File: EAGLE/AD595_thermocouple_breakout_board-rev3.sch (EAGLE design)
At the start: 7 parts

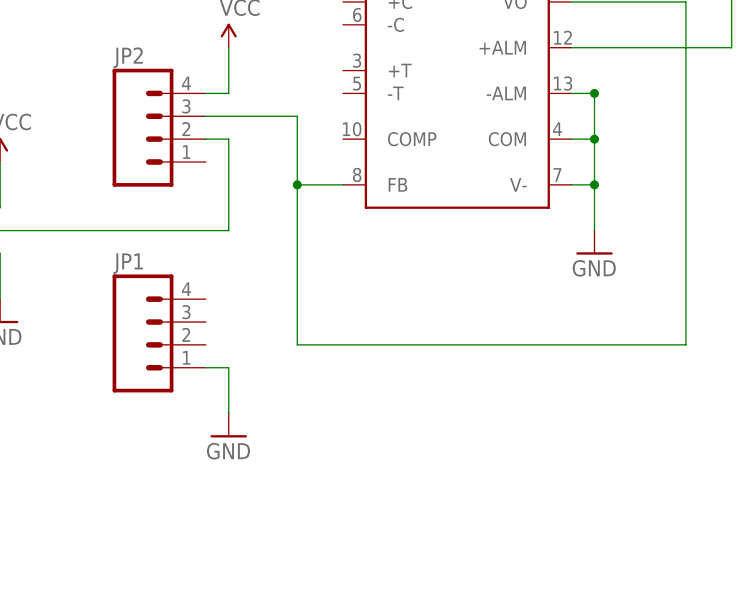
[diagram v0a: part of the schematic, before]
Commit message: Commit of revision three of board. Now includes a program status LED. This version is more part of a toaster reflow oven controller than anything else (hence keeping revision two active).
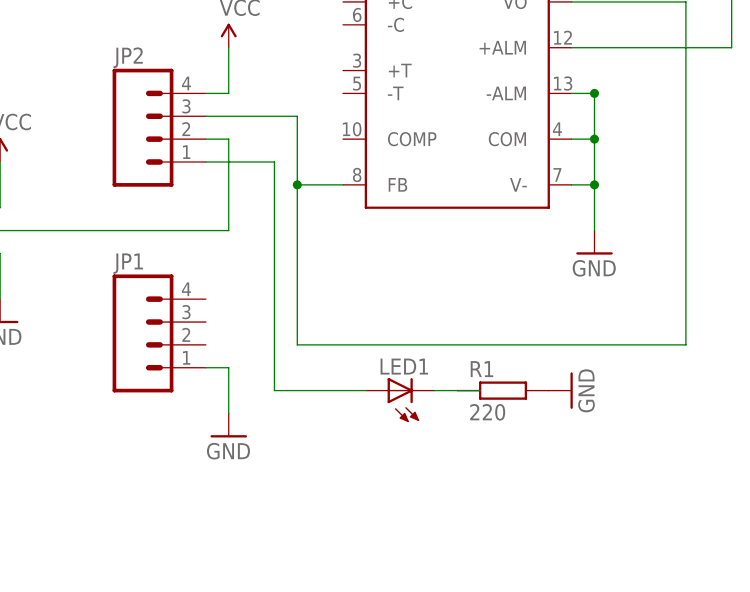
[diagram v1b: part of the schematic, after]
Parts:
- added LED1: (no value), led:LED3MM
- added R1: 220, resistor:R-EU_0207/10
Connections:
- new net N$4: LED1.C, R1.1
- new net N$5: JP2.1, LED1.A
- net GND: now also R1.2
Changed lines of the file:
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@@
 <part name="R2" library="rcl" deviceset="R-US_" device="0207/7" value="330"/>
 <part name="JP3" library="SparkFun-Connectors" deviceset="M03" device="SCREW_LOCK"/>
+<part name="R1" library="resistor" deviceset="R-EU_" device="0207/10" value="220"/>
+<part name="LED1" library="led" deviceset="LED" device="3MM"/>
+<part name="GND4" library="supply1" deviceset="GND" device=""/>
 </parts>
 <sheets>
@@
 <instance part="R2" gate="G$1" x="71.12" y="88.9" rot="R270"/>
 <instance part="JP3" gate="G$1" x="-7.62" y="43.18"/>
+<instance part="R1" gate="G$1" x="58.42" y="25.4"/>
+<instance part="LED1" gate="G$1" x="45.72" y="25.4" rot="R90"/>
+<instance part="GND4" gate="1" x="66.04" y="25.4" rot="R90"/>
 </instances>
 <busses>
@@
 <pinref part="IC1" gate="G$1" pin="-ALM"/>
 <pinref part="GND2" gate="1" pin="GND"/>
+</segment>
+<segment>
+<pinref part="R1" gate="G$1" pin="2"/>
+<pinref part="GND4" gate="1" pin="GND"/>
 </segment>
 </net>
@@
 </segment>
 </net>
+<net name="N$4" class="0">
+<segment>
+<wire x1="50.8" y1="25.4" x2="53.34" y2="25.4" width="0.1524" layer="91"/>
+<wire x1="55.88" y1="25.4" x2="53.34" y2="25.4" width="0.1524" layer="91"/>
+<pinref part="R1" gate="G$1" pin="1"/>
+<pinref part="LED1" gate="G$1" pin="C"/>
+</segment>
+</net>
+<net name="N$5" class="0">
+<segment>
+<wire x1="33.02" y1="25.4" x2="43.18" y2="25.4" width="0.1524" layer="91"/>
+<pinref part="LED1" gate="G$1" pin="A"/>
+<pinref part="JP2" gate="G$1" pin="1"/>
+<wire x1="25.4" y1="50.8" x2="33.02" y2="50.8" width="0.1524" layer="91"/>
+<wire x1="33.02" y1="50.8" x2="33.02" y2="25.4" width="0.1524" layer="91"/>
+</segment>
+</net>

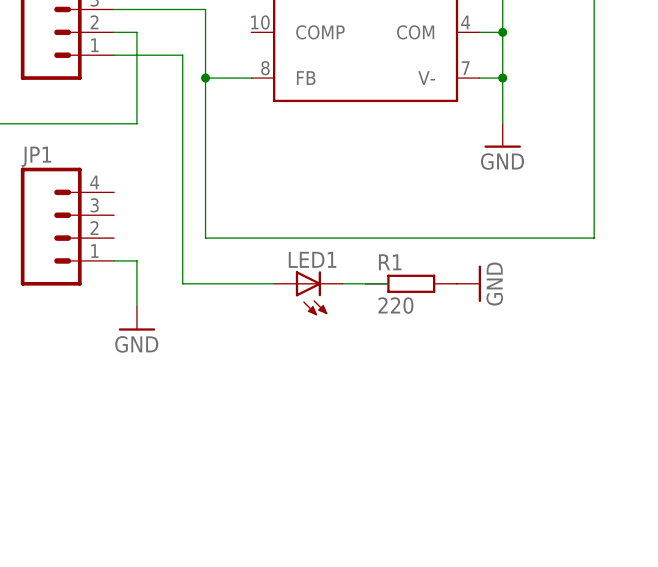
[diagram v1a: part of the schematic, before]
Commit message: Minor change to status LED and resistor in revision 3.
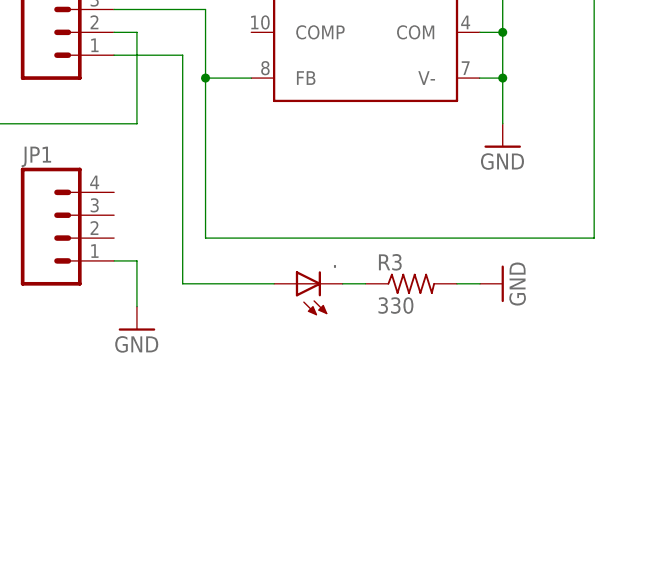
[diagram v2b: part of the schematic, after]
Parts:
- removed LED1: (no value), led:LED3MM
- removed R1: 220, resistor:R-EU_0207/10
- added .: (no value), led:LED5MM
- added R3: 330, rcl:R-US_0207/7
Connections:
- net GND: now also R3.2; no longer R1.2
- net N$4: now also ..C, R3.1; no longer LED1.C, R1.1
- net N$5: now also ..A; no longer LED1.A
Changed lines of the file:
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@@
 <part name="R2" library="rcl" deviceset="R-US_" device="0207/7" value="330"/>
 <part name="JP3" library="SparkFun-Connectors" deviceset="M03" device="SCREW_LOCK"/>
-<part name="R1" library="resistor" deviceset="R-EU_" device="0207/10" value="220"/>
-<part name="LED1" library="led" deviceset="LED" device="3MM"/>
 <part name="GND4" library="supply1" deviceset="GND" device=""/>
+<part name="." library="led" deviceset="LED" device="5MM"/>
+<part name="R3" library="rcl" deviceset="R-US_" device="0207/7" value="330"/>
 </parts>
 <sheets>
@@
 <instance part="R2" gate="G$1" x="71.12" y="88.9" rot="R270"/>
 <instance part="JP3" gate="G$1" x="-7.62" y="43.18"/>
-<instance part="R1" gate="G$1" x="58.42" y="25.4"/>
-<instance part="LED1" gate="G$1" x="45.72" y="25.4" rot="R90"/>
-<instance part="GND4" gate="1" x="66.04" y="25.4" rot="R90"/>
+<instance part="GND4" gate="1" x="68.58" y="25.4" rot="R90"/>
+<instance part="." gate="G$1" x="45.72" y="25.4" rot="R90"/>
+<instance part="R3" gate="G$1" x="58.42" y="25.4"/>
 </instances>
 <busses>
@@
 </segment>
 <segment>
-<pinref part="R1" gate="G$1" pin="2"/>
+<pinref part="R3" gate="G$1" pin="2"/>
 <pinref part="GND4" gate="1" pin="GND"/>
+<wire x1="63.5" y1="25.4" x2="66.04" y2="25.4" width="0.1524" layer="91"/>
 </segment>
 </net>
@@
 <net name="N$4" class="0">
 <segment>
-<wire x1="50.8" y1="25.4" x2="53.34" y2="25.4" width="0.1524" layer="91"/>
-<wire x1="55.88" y1="25.4" x2="53.34" y2="25.4" width="0.1524" layer="91"/>
-<pinref part="R1" gate="G$1" pin="1"/>
-<pinref part="LED1" gate="G$1" pin="C"/>
+<wire x1="53.34" y1="25.4" x2="50.8" y2="25.4" width="0.1524" layer="91"/>
+<pinref part="." gate="G$1" pin="C"/>
+<pinref part="R3" gate="G$1" pin="1"/>
 </segment>
 </net>
@@
 <segment>
 <wire x1="33.02" y1="25.4" x2="43.18" y2="25.4" width="0.1524" layer="91"/>
-<pinref part="LED1" gate="G$1" pin="A"/>
 <pinref part="JP2" gate="G$1" pin="1"/>
 <wire x1="25.4" y1="50.8" x2="33.02" y2="50.8" width="0.1524" layer="91"/>
 <wire x1="33.02" y1="50.8" x2="33.02" y2="25.4" width="0.1524" layer="91"/>
+<pinref part="." gate="G$1" pin="A"/>
 </segment>
 </net>
